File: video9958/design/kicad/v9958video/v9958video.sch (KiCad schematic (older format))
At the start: 25 parts, among them IC1 V9958, IC2 ATF16V8BQL-15, IC3 ATF16V8BQL-15, J1 Conn_02x32_Odd_Even, Q1 21.477MHz, U1 41464, U2 41464, U3 41464, U4 41464, U5 41464, U6 41464

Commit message: First cut PCB
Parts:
- C1, C10, C11, C12, C2, C20, C3, C4, C5, C6, C7, C8, C9: footprint (none) -> Capacitor_THT:C_Rect_L7.0mm_W2.5mm_P5.00mm
- IC1: footprint (none) -> rosco_m68k:sdip64
- IC2, IC3: footprint (none) -> Package_DIP:DIP-20_W7.62mm_LongPads
- Q1: footprint (none) -> rosco_m68k:HC49_S
- R1: footprint (none) -> rosco_m68k:R-0207_10
- U1, U2, U3, U4, U5, U6: footprint (none) -> Package_DIP:DIP-18_W7.62mm_Socket_LongPads
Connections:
- net A1: now also IC2.7 (I7); no longer IC2.9 (I9)
- net A10: now also IC3.16 (IO4); no longer IC3.8 (I8)
- net A11: now also IC3.6 (I6); no longer IC3.9 (I9)
- net A12: now also IC3.15 (IO5); no longer IC3.11 (I10/~OE~)
- net A13: now also IC3.7 (I7); no longer IC3.13 (IO7)
- net A15: now also IC3.8 (I8); no longer IC3.15 (IO5)
- net A16: now also IC3.13 (IO7); no longer IC3.16 (IO4)
- net A17: now also IC3.9 (I9); no longer IC3.17 (I03)
- net A18: now also IC3.11 (I10/~OE~); no longer IC3.18 (IO2)
- net A3: now also IC2.9 (I9); no longer IC2.7 (I7)
- net A6: now also IC3.18 (IO2); no longer IC3.4 (I4)
- net A7: now also IC3.4 (I4); no longer IC3.5 (I5)
- net A8: now also IC3.17 (I03); no longer IC3.6 (I6)
- net A9: now also IC3.5 (I5); no longer IC3.7 (I7)
- net CAS0: now also U5.16 (~CAS), U6.16 (~CAS); no longer U1.16 (~CAS), U2.16 (~CAS)
- net CASX: now also U1.16 (~CAS), U2.16 (~CAS); no longer U5.16 (~CAS), U6.16 (~CAS)
- net VA1: no longer U1.12 (A2)
- net VA2: now also U1.12 (A2)
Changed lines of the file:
@@
 F 0 "IC3" H 7100 2931 50  0000 C CNN
 F 1 "ATF16V8BQL-15" H 7100 2840 50  0000 C CNN
-F 2 "" H 7100 2050 50  0001 C CNN
+F 2 "Package_DIP:DIP-20_W7.62mm_LongPads" H 7100 2050 50  0001 C CNN
 F 3 "" H 7100 2050 50  0001 C CNN
 	1    7100 2050
@@
 F 0 "Q1" H 8950 5132 50  0000 C CNN
 F 1 "21.477MHz" H 8950 5223 50  0000 C CNN
-F 2 "" H 8950 5400 50  0001 C CNN
+F 2 "rosco_m68k:HC49_S" H 8950 5400 50  0001 C CNN
 F 3 "~" H 8950 5400 50  0001 C CNN
 	1    8950 5400
@@
 F 0 "C1" H 8550 5800 50  0000 L CNN
 F 1 "22pF" H 8500 5700 50  0000 L CNN
-F 2 "" H 8838 5600 50  0001 C CNN
+F 2 "Capacitor_THT:C_Rect_L7.0mm_W2.5mm_P5.00mm" H 8838 5600 50  0001 C CNN
 F 3 "~" H 8800 5750 50  0001 C CNN
 	1    8800 5750
@@
 F 0 "C2" H 9215 5796 50  0000 L CNN
 F 1 "22pF" H 9215 5705 50  0000 L CNN
-F 2 "" H 9138 5600 50  0001 C CNN
+F 2 "Capacitor_THT:C_Rect_L7.0mm_W2.5mm_P5.00mm" H 9138 5600 50  0001 C CNN
 F 3 "~" H 9100 5750 50  0001 C CNN
 	1    9100 5750
@@
 FC2
 Text GLabel 4300 2150 0    50   Input ~ 0
-A3
+A1
 Text GLabel 4300 2250 0    50   Input ~ 0
 A2
 Text GLabel 4300 2350 0    50   Input ~ 0
-A1
+A3
 Text GLabel 4300 2450 0    50   Output ~ 0
 ASEL
@@
 F 0 "IC2" H 4800 2931 50  0000 C CNN
 F 1 "ATF16V8BQL-15" H 4800 2840 50  0000 C CNN
-F 2 "" H 4800 2050 50  0001 C CNN
+F 2 "Package_DIP:DIP-20_W7.62mm_LongPads" H 4800 2050 50  0001 C CNN
 F 3 "" H 4800 2050 50  0001 C CNN
 	1    4800 2050
@@
 A5
 Text GLabel 6600 1850 0    50   Input ~ 0
-A6
+A7
 Text GLabel 6600 1950 0    50   Input ~ 0
-A7
+A9
 Text GLabel 6600 2050 0    50   Input ~ 0
-A8
+A11
 Text GLabel 6600 2150 0    50   Input ~ 0
-A9
+A13
 Text GLabel 6600 2250 0    50   Input ~ 0
-A10
+A15
 Text GLabel 6600 2350 0    50   Input ~ 0
-A11
+A17
 Text GLabel 6600 2450 0    50   Input ~ 0
-A12
+A18
 Text GLabel 7600 2150 2    50   Input ~ 0
-A13
+A16
 Text GLabel 7600 2050 2    50   Input ~ 0
 A14
 Text GLabel 7600 1950 2    50   Input ~ 0
-A15
+A12
 Text GLabel 7600 1850 2    50   Input ~ 0
-A16
+A10
 Text GLabel 7600 1750 2    50   Input ~ 0
-A17
+A8
 Text GLabel 7600 1650 2    50   Input ~ 0
-A18
+A6
 Text GLabel 7600 1550 2    50   Output ~ 0
 ASEL
@@
 F 0 "C4" H 8265 2096 50  0000 L CNN
 F 1 "100nF" H 8265 2005 50  0000 L CNN
-F 2 "" H 8188 1900 50  0001 C CNN
+F 2 "Capacitor_THT:C_Rect_L7.0mm_W2.5mm_P5.00mm" H 8188 1900 50  0001 C CNN
 F 3 "~" H 8150 2050 50  0001 C CNN
 	1    8150 2050
@@
 F 0 "C3" H 3715 2046 50  0000 L CNN
 F 1 "100nF" H 3715 1955 50  0000 L CNN
-F 2 "" H 3638 1850 50  0001 C CNN
+F 2 "Capacitor_THT:C_Rect_L7.0mm_W2.5mm_P5.00mm" H 3638 1850 50  0001 C CNN
 F 3 "~" H 3600 2000 50  0001 C CNN
 	1    3600 2000
@@
 Connection ~ 4800 2750
 Text GLabel 1000 5900 0    50   Input ~ 0
-CAS0
+CASX
 Text GLabel 1000 7600 0    50   Input ~ 0
-CAS0
+CASX
 Text GLabel 2850 5900 0    50   Input ~ 0
 CAS1
@@
 CAS1
 Text GLabel 4750 5900 0    50   Input ~ 0
-CASX
+CAS0
 Text GLabel 4750 7600 0    50   Input ~ 0
-CASX
+CAS0
 Text GLabel 2200 4700 2    50   BiDi ~ 0
 VD0
@@
 F 0 "C5" H 3165 3846 50  0000 L CNN
 F 1 "100nF" H 3165 3755 50  0000 L CNN
-F 2 "" H 3088 3650 50  0001 C CNN
+F 2 "Capacitor_THT:C_Rect_L7.0mm_W2.5mm_P5.00mm" H 3088 3650 50  0001 C CNN
 F 3 "~" H 3050 3800 50  0001 C CNN
 	1    3050 3800
@@
 F 0 "C6" H 3515 3846 50  0000 L CNN
 F 1 "100nF" H 3515 3755 50  0000 L CNN
-F 2 "" H 3438 3650 50  0001 C CNN
+F 2 "Capacitor_THT:C_Rect_L7.0mm_W2.5mm_P5.00mm" H 3438 3650 50  0001 C CNN
 F 3 "~" H 3400 3800 50  0001 C CNN
 	1    3400 3800
@@
 F 0 "C7" H 3865 3846 50  0000 L CNN
 F 1 "100nF" H 3865 3755 50  0000 L CNN
-F 2 "" H 3788 3650 50  0001 C CNN
+F 2 "Capacitor_THT:C_Rect_L7.0mm_W2.5mm_P5.00mm" H 3788 3650 50  0001 C CNN
 F 3 "~" H 3750 3800 50  0001 C CNN
 	1    3750 3800
@@
 F 0 "C8" H 4215 3846 50  0000 L CNN
 F 1 "100nF" H 4215 3755 50  0000 L CNN
-F 2 "" H 4138 3650 50  0001 C CNN
+F 2 "Capacitor_THT:C_Rect_L7.0mm_W2.5mm_P5.00mm" H 4138 3650 50  0001 C CNN
 F 3 "~" H 4100 3800 50  0001 C CNN
 	1    4100 3800
@@
 F 0 "C9" H 4565 3846 50  0000 L CNN
 F 1 "100nF" H 4565 3755 50  0000 L CNN
-F 2 "" H 4488 3650 50  0001 C CNN
+F 2 "Capacitor_THT:C_Rect_L7.0mm_W2.5mm_P5.00mm" H 4488 3650 50  0001 C CNN
 F 3 "~" H 4450 3800 50  0001 C CNN
 	1    4450 3800
@@
 F 0 "C10" H 4915 3846 50  0000 L CNN
 F 1 "100nF" H 4915 3755 50  0000 L CNN
-F 2 "" H 4838 3650 50  0001 C CNN
+F 2 "Capacitor_THT:C_Rect_L7.0mm_W2.5mm_P5.00mm" H 4838 3650 50  0001 C CNN
 F 3 "~" H 4800 3800 50  0001 C CNN
 	1    4800 3800
@@
 F 0 "C11" H 5565 3846 50  0000 L CNN
 F 1 "100nF" H 5565 3755 50  0000 L CNN
-F 2 "" H 5488 3650 50  0001 C CNN
+F 2 "Capacitor_THT:C_Rect_L7.0mm_W2.5mm_P5.00mm" H 5488 3650 50  0001 C CNN
 F 3 "~" H 5450 3800 50  0001 C CNN
 	1    5450 3800
@@
 F 0 "C12" H 5915 3846 50  0000 L CNN
 F 1 "100nF" H 5915 3755 50  0000 L CNN
-F 2 "" H 5838 3650 50  0001 C CNN
+F 2 "Capacitor_THT:C_Rect_L7.0mm_W2.5mm_P5.00mm" H 5838 3650 50  0001 C CNN
 F 3 "~" H 5800 3800 50  0001 C CNN
 	1    5800 3800
@@
 F 0 "R1" H 8670 2846 50  0000 L CNN
 F 1 "4K7" H 8670 2755 50  0000 L CNN
-F 2 "" V 8530 2800 50  0001 C CNN
+F 2 "rosco_m68k:R-0207_10" V 8530 2800 50  0001 C CNN
 F 3 "~" H 8600 2800 50  0001 C CNN
 	1    8600 2800
@@
 VA0
 Text GLabel 1000 4900 0    50   Input ~ 0
-VA1
+VA2
 Text GLabel 1000 5200 0    50   Input ~ 0
 VA5
@@
 F 0 "C20" H 10865 5496 50  0000 L CNN
 F 1 "100nF" H 10865 5405 50  0000 L CNN
-F 2 "" H 10788 5300 50  0001 C CNN
+F 2 "Capacitor_THT:C_Rect_L7.0mm_W2.5mm_P5.00mm" H 10788 5300 50  0001 C CNN
 F 3 "~" H 10750 5450 50  0001 C CNN
 	1    10750 5450
@@
 F 0 "IC1" H 9850 4881 50  0000 C CNN
 F 1 "V9958" H 9850 4790 50  0000 C CNN
-F 2 "" H 9850 3750 50  0000 C CNN
-F 3 "" H 9850 3750 50  0000 C CNN
+F 2 "rosco_m68k:sdip64" H 9850 3750 50  0001 C CNN
+F 3 "http://map.grauw.nl/resources/video/yamaha_v9958_ocr.pdf" H 9750 5700 50  0000 C CNN
 	1    9850 3200
 	1    0    0    -1
@@
 F 0 "U1" H 1600 6731 50  0000 C CNN
 F 1 "41464" H 1600 6640 50  0000 C CNN
-F 2 "" H 1700 5600 50  0000 C CNN
-F 3 "" H 1700 5600 50  0000 C CNN
+F 2 "Package_DIP:DIP-18_W7.62mm_Socket_LongPads" H 1700 5600 50  0001 C CNN
+F 3 "https://downloads.reactivemicro.com/Electronics/DRAM/NEC%20D41464%2064k%20x%204bit%20DRAM%20Data%20Sheet.pdf" H 1700 5600 50  0001 C CNN
 	1    1600 5600
 	1    0    0    -1
@@
 F 0 "U2" H 1600 8431 50  0000 C CNN
 F 1 "41464" H 1600 8340 50  0000 C CNN
-F 2 "" H 1700 7300 50  0000 C CNN
-F 3 "" H 1700 7300 50  0000 C CNN
+F 2 "Package_DIP:DIP-18_W7.62mm_Socket_LongPads" H 1700 7300 50  0001 C CNN
+F 3 "https://downloads.reactivemicro.com/Electronics/DRAM/NEC%20D41464%2064k%20x%204bit%20DRAM%20Data%20Sheet.pdf" H 1700 7300 50  0001 C CNN
 	1    1600 7300
 	1    0    0    -1
@@
 F 0 "U3" H 3450 6731 50  0000 C CNN
 F 1 "41464" H 3450 6640 50  0000 C CNN
-F 2 "" H 3550 5600 50  0000 C CNN
-F 3 "" H 3550 5600 50  0000 C CNN
+F 2 "Package_DIP:DIP-18_W7.62mm_Socket_LongPads" H 3550 5600 50  0001 C CNN
+F 3 "https://downloads.reactivemicro.com/Electronics/DRAM/NEC%20D41464%2064k%20x%204bit%20DRAM%20Data%20Sheet.pdf" H 3550 5600 50  0001 C CNN
 	1    3450 5600
 	1    0    0    -1
@@
 F 0 "U4" H 3450 8431 50  0000 C CNN
 F 1 "41464" H 3450 8340 50  0000 C CNN
-F 2 "" H 3550 7300 50  0000 C CNN
-F 3 "" H 3550 7300 50  0000 C CNN
+F 2 "Package_DIP:DIP-18_W7.62mm_Socket_LongPads" H 3550 7300 50  0001 C CNN
+F 3 "https://downloads.reactivemicro.com/Electronics/DRAM/NEC%20D41464%2064k%20x%204bit%20DRAM%20Data%20Sheet.pdf" H 3550 7300 50  0001 C CNN
 	1    3450 7300
 	1    0    0    -1
@@
 F 0 "U5" H 5350 6731 50  0000 C CNN
 F 1 "41464" H 5350 6640 50  0000 C CNN
-F 2 "" H 5450 5600 50  0000 C CNN
-F 3 "" H 5450 5600 50  0000 C CNN
+F 2 "Package_DIP:DIP-18_W7.62mm_Socket_LongPads" H 5450 5600 50  0001 C CNN
+F 3 "https://downloads.reactivemicro.com/Electronics/DRAM/NEC%20D41464%2064k%20x%204bit%20DRAM%20Data%20Sheet.pdf" H 5450 5600 50  0001 C CNN
 	1    5350 5600
 	1    0    0    -1
@@
 F 0 "U6" H 5350 8431 50  0000 C CNN
 F 1 "41464" H 5350 8340 50  0000 C CNN
-F 2 "" H 5450 7300 50  0000 C CNN
-F 3 "" H 5450 7300 50  0000 C CNN
+F 2 "Package_DIP:DIP-18_W7.62mm_Socket_LongPads" H 5450 7300 50  0001 C CNN
+F 3 "https://downloads.reactivemicro.com/Electronics/DRAM/NEC%20D41464%2064k%20x%204bit%20DRAM%20Data%20Sheet.pdf" H 3250 8550 50  0000 C CNN
 	1    5350 7300
 	1    0    0    -1

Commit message: First round fixes
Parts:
- renumbered C5 to C1, C4 to C10, C1 to C11, C2 to C12, C20 to C13, C6 to C2, C7 to C4, C8 to C5, C9 to C6, C10 to C7, C11 to C8, C12 to C9, IC2 to IC1, IC3 to IC2, IC1 to IC3
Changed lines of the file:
@@
 $EndDescr
 $Comp
-L Logic_Programmable:GAL16V8 IC3
+L Logic_Programmable:GAL16V8 IC2
 U 1 1 5EAF7BFD
 P 7100 2050
-F 0 "IC3" H 7100 2931 50  0000 C CNN
+F 0 "IC2" H 7100 2931 50  0000 C CNN
 F 1 "ATF16V8BQL-15" H 7100 2840 50  0000 C CNN
 F 2 "Package_DIP:DIP-20_W7.62mm_LongPads" H 7100 2050 50  0001 C CNN
@@
 BIGOR.PLD
 $Comp
-L Device:C C1
+L Device:C C11
 U 1 1 5EAFB883
 P 8800 5750
-F 0 "C1" H 8550 5800 50  0000 L CNN
+F 0 "C11" H 8550 5800 50  0000 L CNN
 F 1 "22pF" H 8500 5700 50  0000 L CNN
 F 2 "Capacitor_THT:C_Rect_L7.0mm_W2.5mm_P5.00mm" H 8838 5600 50  0001 C CNN
@@
 $EndComp
 $Comp
-L Device:C C2
+L Device:C C12
 U 1 1 5EAFC3D1
 P 9100 5750
-F 0 "C2" H 9215 5796 50  0000 L CNN
+F 0 "C12" H 9215 5796 50  0000 L CNN
 F 1 "22pF" H 9215 5705 50  0000 L CNN
 F 2 "Capacitor_THT:C_Rect_L7.0mm_W2.5mm_P5.00mm" H 9138 5600 50  0001 C CNN
@@
 RnW
 $Comp
-L power:PWR_FLAG #GND0101
+L power:PWR_FLAG #GND01
 U 1 1 5EB06E7A
 P 950 1100
-F 0 "#GND0101" H 950 1175 50  0001 C CNN
+F 0 "#GND01" H 950 1175 50  0001 C CNN
 F 1 "PWR_FLAG" H 950 1273 50  0001 C CNN
 F 2 "" H 950 1100 50  0001 C CNN
@@
 $EndComp
 $Comp
-L power:PWR_FLAG #VCC0101
+L power:PWR_FLAG #VCC01
 U 1 1 5EB06E82
 P 950 850
-F 0 "#VCC0101" H 950 925 50  0001 C CNN
+F 0 "#VCC01" H 950 925 50  0001 C CNN
 F 1 "PWR_FLAG" H 950 1023 50  0001 C CNN
 F 2 "" H 950 850 50  0001 C CNN
@@
 ASEL
 $Comp
-L Logic_Programmable:GAL16V8 IC2
+L Logic_Programmable:GAL16V8 IC1
 U 1 1 5EAF6AE7
 P 4800 2050
-F 0 "IC2" H 4800 2931 50  0000 C CNN
+F 0 "IC1" H 4800 2931 50  0000 C CNN
 F 1 "ATF16V8BQL-15" H 4800 2840 50  0000 C CNN
 F 2 "Package_DIP:DIP-20_W7.62mm_LongPads" H 4800 2050 50  0001 C CNN
@@
 Connection ~ 7100 1350
 $Comp
-L Device:C C4
+L Device:C C10
 U 1 1 5EB5B26B
 P 8150 2050
-F 0 "C4" H 8265 2096 50  0000 L CNN
+F 0 "C10" H 8265 2096 50  0000 L CNN
 F 1 "100nF" H 8265 2005 50  0000 L CNN
 F 2 "Capacitor_THT:C_Rect_L7.0mm_W2.5mm_P5.00mm" H 8188 1900 50  0001 C CNN
@@
 NoConn ~ 10550 4100
 $Comp
-L Device:C C5
+L Device:C C1
 U 1 1 5EBD6A2D
 P 3050 3800
-F 0 "C5" H 3165 3846 50  0000 L CNN
+F 0 "C1" H 3165 3846 50  0000 L CNN
 F 1 "100nF" H 3165 3755 50  0000 L CNN
 F 2 "Capacitor_THT:C_Rect_L7.0mm_W2.5mm_P5.00mm" H 3088 3650 50  0001 C CNN
@@
 $EndComp
 $Comp
-L Device:C C6
+L Device:C C2
 U 1 1 5EBD70D8
 P 3400 3800
-F 0 "C6" H 3515 3846 50  0000 L CNN
+F 0 "C2" H 3515 3846 50  0000 L CNN
 F 1 "100nF" H 3515 3755 50  0000 L CNN
 F 2 "Capacitor_THT:C_Rect_L7.0mm_W2.5mm_P5.00mm" H 3438 3650 50  0001 C CNN
@@
 $EndComp
 $Comp
-L Device:C C7
+L Device:C C4
 U 1 1 5EBD76DD
 P 3750 3800
-F 0 "C7" H 3865 3846 50  0000 L CNN
+F 0 "C4" H 3865 3846 50  0000 L CNN
 F 1 "100nF" H 3865 3755 50  0000 L CNN
 F 2 "Capacitor_THT:C_Rect_L7.0mm_W2.5mm_P5.00mm" H 3788 3650 50  0001 C CNN
@@
 $EndComp
 $Comp
-L Device:C C8
+L Device:C C5
 U 1 1 5EBD7BDB
 P 4100 3800
-F 0 "C8" H 4215 3846 50  0000 L CNN
+F 0 "C5" H 4215 3846 50  0000 L CNN
 F 1 "100nF" H 4215 3755 50  0000 L CNN
 F 2 "Capacitor_THT:C_Rect_L7.0mm_W2.5mm_P5.00mm" H 4138 3650 50  0001 C CNN
@@
 $EndComp
 $Comp
-L Device:C C9
+L Device:C C6
 U 1 1 5EBD8054
 P 4450 3800
-F 0 "C9" H 4565 3846 50  0000 L CNN
+F 0 "C6" H 4565 3846 50  0000 L CNN
 F 1 "100nF" H 4565 3755 50  0000 L CNN
 F 2 "Capacitor_THT:C_Rect_L7.0mm_W2.5mm_P5.00mm" H 4488 3650 50  0001 C CNN
@@
 $EndComp
 $Comp
-L Device:C C10
+L Device:C C7
 U 1 1 5EBD8730
 P 4800 3800
-F 0 "C10" H 4915 3846 50  0000 L CNN
+F 0 "C7" H 4915 3846 50  0000 L CNN
 F 1 "100nF" H 4915 3755 50  0000 L CNN
 F 2 "Capacitor_THT:C_Rect_L7.0mm_W2.5mm_P5.00mm" H 4838 3650 50  0001 C CNN
@@
 $EndComp
 $Comp
-L Device:C C11
+L Device:C C8
 U 1 1 5EBD902F
 P 5450 3800
-F 0 "C11" H 5565 3846 50  0000 L CNN
+F 0 "C8" H 5565 3846 50  0000 L CNN
 F 1 "100nF" H 5565 3755 50  0000 L CNN
 F 2 "Capacitor_THT:C_Rect_L7.0mm_W2.5mm_P5.00mm" H 5488 3650 50  0001 C CNN
@@
 $EndComp
 $Comp
-L Device:C C12
+L Device:C C9
 U 1 1 5EBD97B4
 P 5800 3800
-F 0 "C12" H 5915 3846 50  0000 L CNN
+F 0 "C9" H 5915 3846 50  0000 L CNN
 F 1 "100nF" H 5915 3755 50  0000 L CNN
 F 2 "Capacitor_THT:C_Rect_L7.0mm_W2.5mm_P5.00mm" H 5838 3650 50  0001 C CNN
@@
 	10750 5050 10750 5300
 $Comp
-L Device:C C20
+L Device:C C13
 U 1 1 5ECA6BAF
 P 10750 5450
-F 0 "C20" H 10865 5496 50  0000 L CNN
+F 0 "C13" H 10865 5496 50  0000 L CNN
 F 1 "100nF" H 10865 5405 50  0000 L CNN
 F 2 "Capacitor_THT:C_Rect_L7.0mm_W2.5mm_P5.00mm" H 10788 5300 50  0001 C CNN
@@
 	10100 1300 10100 1700
 $Comp
-L rosco_m68k:V9958 IC1
+L rosco_m68k:V9958 IC3
 U 1 1 5EDA9097
 P 9850 3200
-F 0 "IC1" H 9850 4881 50  0000 C CNN
+F 0 "IC3" H 9850 4881 50  0000 C CNN
 F 1 "V9958" H 9850 4790 50  0000 C CNN
 F 2 "rosco_m68k:sdip64" H 9850 3750 50  0001 C CNN

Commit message: Rev 1 - Four layer board
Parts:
- added C14, C15: 100uF, Capacitor_THT:CP_Radial_D5.0mm_P2.50mm, symbol Device:CP
- renumbered C9 to C10, C13 to C11, C11 to C12, C12 to C13, C4 to C3, C5 to C4, C6 to C5, C7 to C6, C3 to C7, C10 to C8, C8 to C9
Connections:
- net GND: now also C14.2, C15.2
- net VCC: now also C14.1, C15.1
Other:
- moved on the sheet: C1, C10, C2, C3, C4, C5, C6, C9

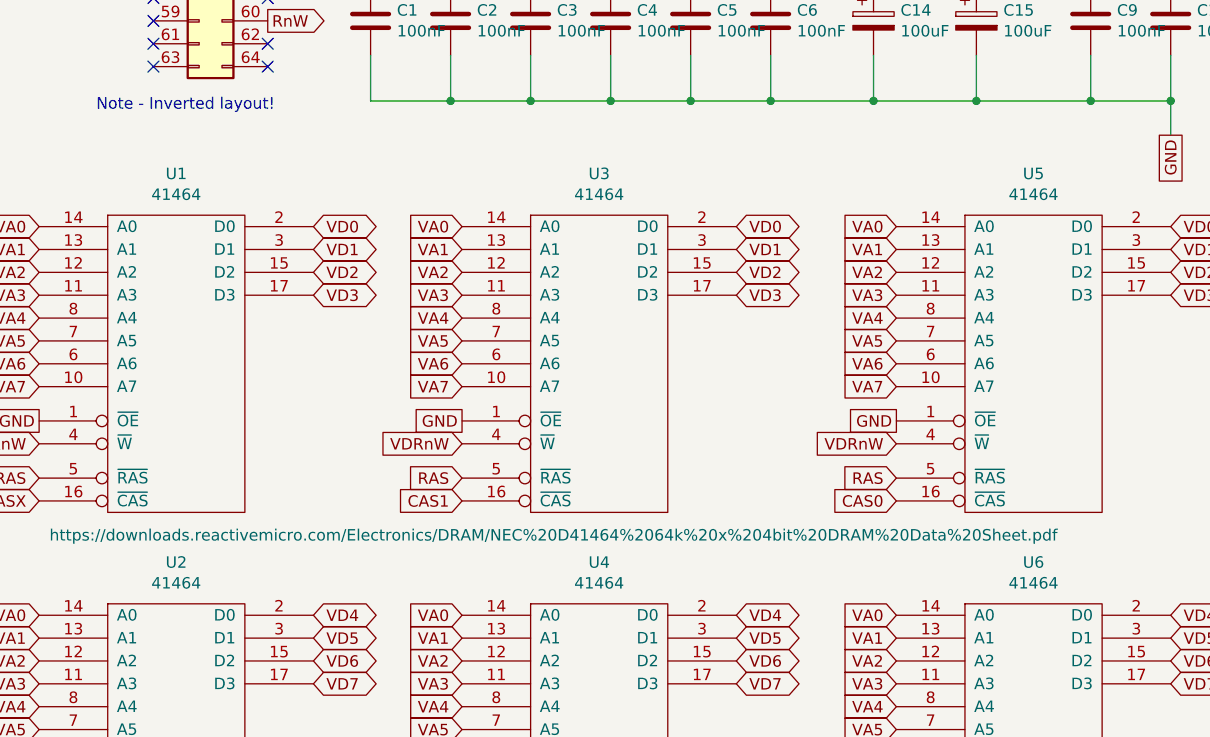
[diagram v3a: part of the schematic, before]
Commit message: Make IC numbering less nonsensical
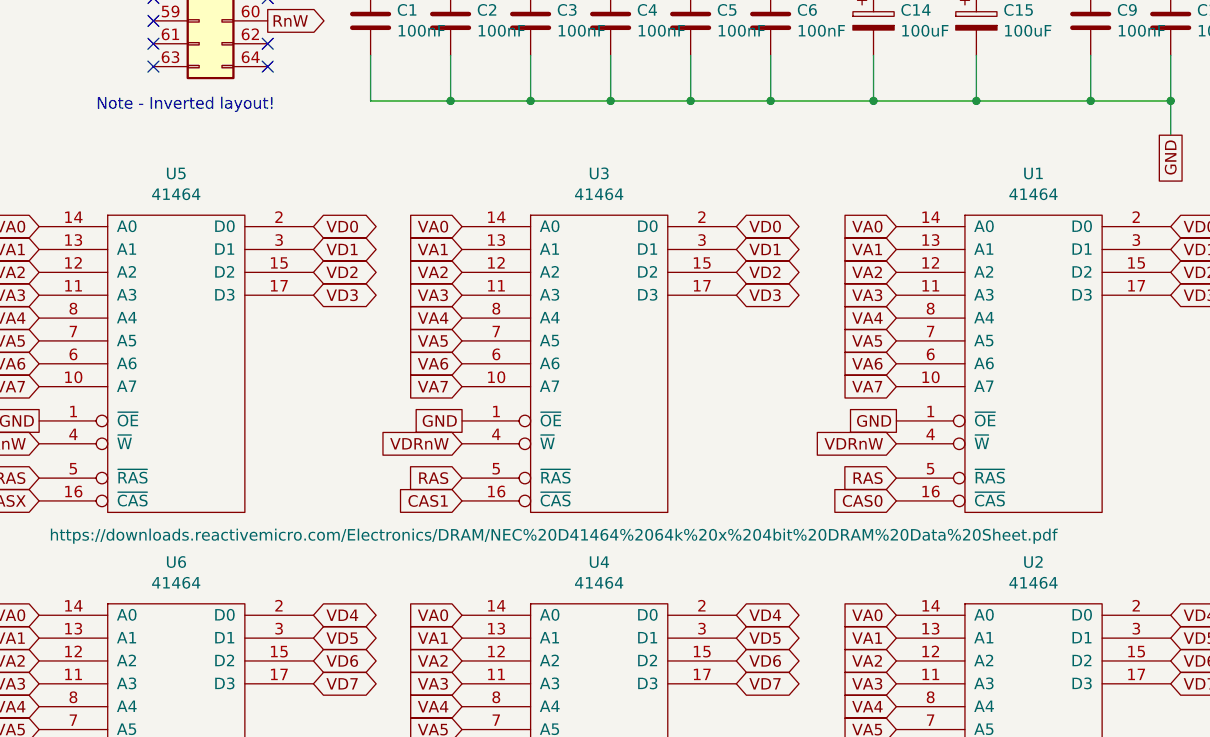
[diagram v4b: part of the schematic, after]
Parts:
- renumbered U5 to U1, U6 to U2, U1 to U5, U2 to U6
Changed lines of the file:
@@
 $EndComp
 $Comp
-L rosco_m68k:41464 U1
+L rosco_m68k:41464 U5
 U 1 1 5EDB033D
 P 1600 5600
-F 0 "U1" H 1600 6731 50  0000 C CNN
+F 0 "U5" H 1600 6731 50  0000 C CNN
 F 1 "41464" H 1600 6640 50  0000 C CNN
 F 2 "Package_DIP:DIP-18_W7.62mm_Socket_LongPads" H 1700 5600 50  0001 C CNN
@@
 $EndComp
 $Comp
-L rosco_m68k:41464 U2
+L rosco_m68k:41464 U6
 U 1 1 5EDB1569
 P 1600 7300
-F 0 "U2" H 1600 8431 50  0000 C CNN
+F 0 "U6" H 1600 8431 50  0000 C CNN
 F 1 "41464" H 1600 8340 50  0000 C CNN
 F 2 "Package_DIP:DIP-18_W7.62mm_Socket_LongPads" H 1700 7300 50  0001 C CNN
@@
 $EndComp
 $Comp
-L rosco_m68k:41464 U5
+L rosco_m68k:41464 U1
 U 1 1 5EDB48B2
 P 5350 5600
-F 0 "U5" H 5350 6731 50  0000 C CNN
+F 0 "U1" H 5350 6731 50  0000 C CNN
 F 1 "41464" H 5350 6640 50  0000 C CNN
 F 2 "Package_DIP:DIP-18_W7.62mm_Socket_LongPads" H 5450 5600 50  0001 C CNN
@@
 $EndComp
 $Comp
-L rosco_m68k:41464 U6
+L rosco_m68k:41464 U2
 U 1 1 5EDB566C
 P 5350 7300
-F 0 "U6" H 5350 8431 50  0000 C CNN
+F 0 "U2" H 5350 8431 50  0000 C CNN
 F 1 "41464" H 5350 8340 50  0000 C CNN
 F 2 "Package_DIP:DIP-18_W7.62mm_Socket_LongPads" H 5450 7300 50  0001 C CNN

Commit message: Revision 1.1 RTM
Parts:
- added C27, C28: 100nF, Capacitor_THT:C_Rect_L7.0mm_W2.5mm_P5.00mm, symbol Device:C
- C15: value 100uF -> 220uF; footprint Capacitor_THT:CP_Radial_D5.0mm_P2.50mm -> Capacitor_THT:CP_Radial_D6.3mm_P2.50mm
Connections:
- net GND: now also C27.2, C28.2
- net VCC: now also C27.1, C28.1
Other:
- moved on the sheet: C8
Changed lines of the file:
@@
 L Device:C C8
 U 1 1 5EB5B26B
-P 8150 2050
-F 0 "C8" H 8265 2096 50  0000 L CNN
-F 1 "100nF" H 8265 2005 50  0000 L CNN
-F 2 "Capacitor_THT:C_Rect_L7.0mm_W2.5mm_P5.00mm" H 8188 1900 50  0001 C CNN
-F 3 "~" H 8150 2050 50  0001 C CNN
-	1    8150 2050
+P 8150 2000
+F 0 "C8" H 8265 2046 50  0000 L CNN
+F 1 "100nF" H 8265 1955 50  0000 L CNN
+F 2 "Capacitor_THT:C_Rect_L7.0mm_W2.5mm_P5.00mm" H 8188 1850 50  0001 C CNN
+F 3 "~" H 8150 2000 50  0001 C CNN
+	1    8150 2000
 	1    0    0    -1
 $EndComp
@@
 $EndComp
 Wire Wire Line
-	8150 1350 8150 1900
-Wire Wire Line
 	8150 2750 7100 2750
 Connection ~ 7100 2750
-Wire Wire Line
-	8150 2200 8150 2750
 Wire Wire Line
 	3600 1850 3600 1350
@@
 F11 "EXT_VIDEO" I R 7900 4250 50
 $EndSheet
-Wire Wire Line
-	7050 3750 6550 3750
-Wire Wire Line
-	6550 3550 7050 3550
-Text GLabel 6550 3550 0    50   UnSpc ~ 0
+Text GLabel 6950 3550 0    50   UnSpc ~ 0
 VCC
-Text GLabel 6550 3750 0    50   UnSpc ~ 0
+Text GLabel 6950 3750 0    50   UnSpc ~ 0
 GND
 NoConn ~ 9150 4650
@@
 P 5100 3800
 F 0 "C15" H 5218 3846 50  0000 L CNN
-F 1 "100uF" H 5218 3755 50  0000 L CNN
-F 2 "Capacitor_THT:CP_Radial_D5.0mm_P2.50mm" H 5138 3650 50  0001 C CNN
+F 1 "220uF" H 5218 3755 50  0000 L CNN
+F 2 "Capacitor_THT:CP_Radial_D6.3mm_P2.50mm" H 5138 3650 50  0001 C CNN
 F 3 "~" H 5100 3800 50  0001 C CNN
 	1    5100 3800
@@
 Wire Wire Line
 	4650 4150 5100 4150
+$Comp
+L Device:C C28
+U 1 1 5EDA8065
+P 5950 2000
+F 0 "C28" H 6065 2046 50  0000 L CNN
+F 1 "100nF" H 6065 1955 50  0000 L CNN
+F 2 "Capacitor_THT:C_Rect_L7.0mm_W2.5mm_P5.00mm" H 5988 1850 50  0001 C CNN
+F 3 "~" H 5950 2000 50  0001 C CNN
+	1    5950 2000
+	1    0    0    -1
+$EndComp
+Wire Wire Line
+	8150 1850 8150 1350
+Wire Wire Line
+	8150 2150 8150 2750
+Wire Wire Line
+	5950 1850 5950 1350
+Wire Wire Line
+	5950 2150 5950 2750
+Wire Wire Line
+	6950 3550 7050 3550
+Wire Wire Line
+	6950 3750 7050 3750
+$Comp
+L Device:C C27
+U 1 1 5EDDDA3B
+P 6400 3800
+F 0 "C27" H 6515 3846 50  0000 L CNN
+F 1 "100nF" H 6515 3755 50  0000 L CNN
+F 2 "Capacitor_THT:C_Rect_L7.0mm_W2.5mm_P5.00mm" H 6438 3650 50  0001 C CNN
+F 3 "~" H 6400 3800 50  0001 C CNN
+	1    6400 3800
+	1    0    0    -1
+$EndComp
+Wire Wire Line
+	6400 3650 6400 3450
+Wire Wire Line
+	6400 3450 5950 3450
+Connection ~ 5950 3450
+Wire Wire Line
+	5950 4150 6400 4150
+Wire Wire Line
+	6400 4150 6400 3950
 $EndSCHEMATC
